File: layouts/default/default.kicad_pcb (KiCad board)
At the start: 2 copper layers, 40.8 x 45.9 mm, 62 parts, among them U10 10µF ±10% 25V X5R, U11 10µF ±10% 25V X5R, U12 10µF ±10% 25V X5R, U13 1MΩ ±1% 62.5mW, U14 100nF ±10% 16V X7R, U16 1µF ±10% 25V X5R, U17 560Ω ±1% 62.5mW, U18 1µF ±10% 25V X5R, U19 4.7kΩ ±1% 62.5mW, U20 10µF ±10% 25V X5R, U21 10µF ±10% 25V X5R, U23 10kΩ ±1% 62.5mW, U25 100nF ±10% 16V X7R, U29 4.7kΩ ±1% 62.5mW, U5 100kΩ ±1% 62.5mW, U6 560kΩ ±1% 62.5mW, U8 1.5µH ±20%, U9 10µF ±10% 25V X5R

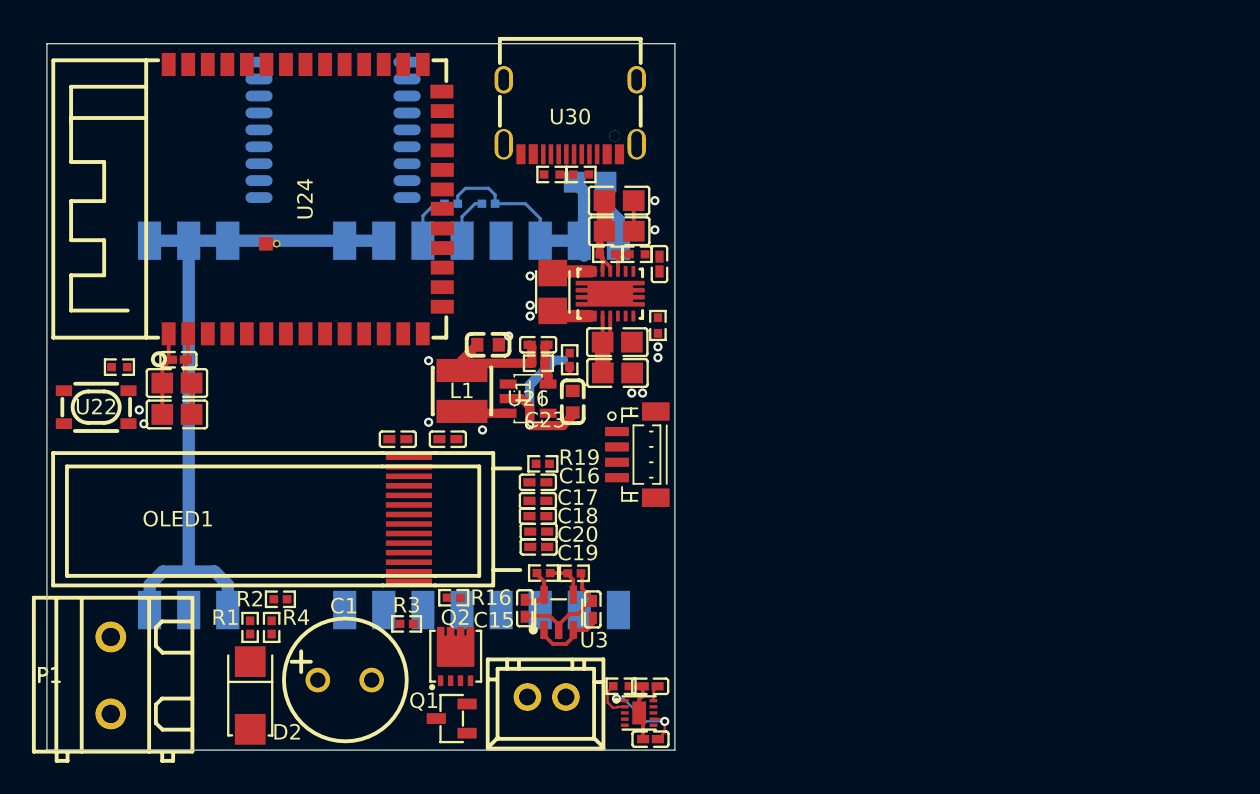
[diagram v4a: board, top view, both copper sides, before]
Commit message: update before removing oled
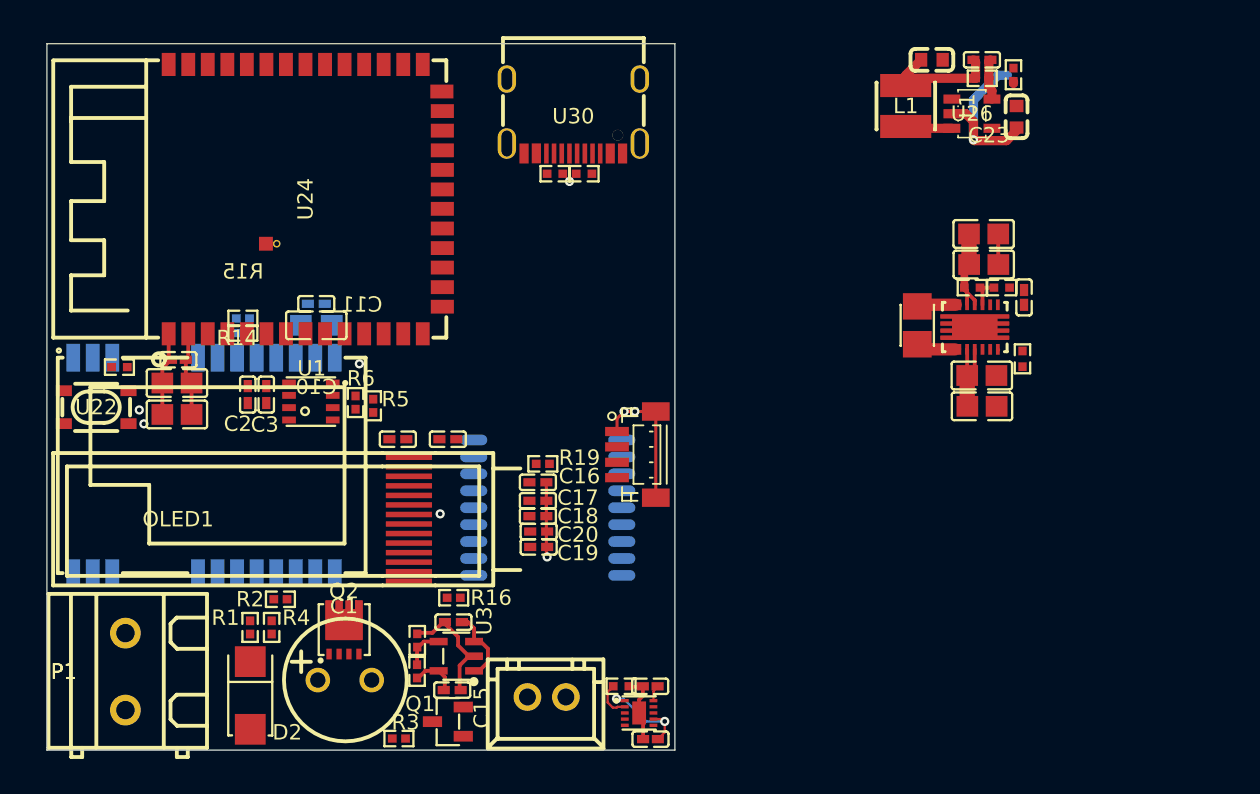
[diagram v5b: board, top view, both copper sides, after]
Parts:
- added C2: 100nF ±10% 16V X7R, atopile:C0402-b3ef17, F.Cu at (46.9, 56.5)
- added C3: 100nF ±10% 16V X7R, atopile:C0402-b3ef17, F.Cu at (48.0, 56.5)
- added R5: 1kΩ ±1% 62.5mW, atopile:R0402-56259e, F.Cu at (55.0, 57.2)
- added R6: 1kΩ ±1% 62.5mW, atopile:R0402-56259e, F.Cu at (53.9, 57.0)
- added U1: , atopile:LGA-8_L3.0-W3.0-P0.80_BME688-7465bb, F.Cu at (51.0, 57.0)
- R1, R14, R15, R2, R3, R4, U5: value 100kΩ ±1% 62.5mW -> 1kΩ ±1% 62.5mW
- R16: value 510kΩ ±1% 62.5mW -> 560kΩ ±1% 62.5mW
- U2: footprint atopile:WIRELM-SMD_E22-900M30S-98c301 -> atopile:WIRELM-SMD_E22-900M22S-72e54e
- U6: value 560kΩ ±1% 62.5mW -> 5.6kΩ ±1% 62.5mW
- moved U26 34.3 mm to (93.9, 38.2)
- moved C22 34.3 mm to (94.5, 34.8)
- moved C23 34.3 mm to (96.8, 38.5)
- moved C24 34.3 mm to (91.3, 34.8)
- moved L1 34.3 mm to (89.6, 37.8)
- moved R20 34.3 mm to (96.6, 35.7)
- moved R21 34.3 mm to (94.6, 36.0)
- moved U27 28.2 mm to (66.3, 63.9)
- moved U10 23.8 mm to (94.6, 57.3)
- moved U11 23.8 mm to (94.7, 48.0)
- moved U13 23.8 mm to (97.2, 54.2)
- moved U14 23.8 mm to (97.3, 50.2)
- moved U5 23.8 mm to (95.8, 49.5)
- moved U9 23.8 mm to (94.5, 55.3)
- moved U12 23.8 mm to (94.7, 46.1)
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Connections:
- C15 pad 1: hv-1 -> hv
- C16 pad 1: hv-3 -> hv-1
- C17 pad 1: hv-3 -> hv-1
- C18 pad 1: hv-3 -> hv-1
- C19 pad 1: hv-3 -> hv-1
- C20 pad 1: hv-3 -> hv-1
- C22 pad 1: hv-3 -> hv-1
- C23 pad 1: hv -> hv-3
- C24 pad 1: hv-3 -> hv-1
- CN1 pad 1: hv -> hv-3
- CN2 pad 2: hv-3 -> hv-1
- L1 pad 2: hv-3 -> hv-1
- OLED1 pad 13: hv-3 -> hv-1
- OLED1 pad 14: hv-3 -> hv-1
- OLED1 pad 5: hv-1 -> hv
- OLED1 pad 8: hv-3 -> hv-1
- R18 pad 1: hv-1 -> hv
- R19 pad 2: hv-3 -> hv-1
- R21 pad 1: hv-3 -> hv-1
- U10 pad 1: hv -> hv-3
- U15 pad 10: hv -> hv-3
- U18 pad 1: hv -> hv-3
- U2 pad 10: hv-2 -> gnd
- U20 pad 1: hv-3 -> hv-1
- U21 pad 1: hv-3 -> hv-1
- U23 pad 1: hv-3 -> hv-1
- U24 pad 2: hv-3 -> hv-1
- U25 pad 1: hv-3 -> hv-1
- U26 pad 4: hv -> hv-3
- U27 pad 14: hv-3 -> hv-1
- U27 pad 8: hv-3 -> hv-1
- U3 pad 5: hv-1 -> hv
- U7 pad 10: hv -> hv-3
- U7 pad 11: hv -> hv-3
- U9 pad 1: hv -> hv-3
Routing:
- net gnd: track 82.0 -> 46.2 mm, vias 16 -> 9
- net hv-2: track 35.5 -> 17.7 mm
- net hv-1: track 3.05 -> 13.5 mm
- net hv-3: track 13.5 -> 6.80 mm
- net RXEN: track 4.05 -> 0.00 mm
- net hv: track 6.80 -> 3.05 mm
- net TXEN: track 3.23 -> 0.00 mm

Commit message: desktop push
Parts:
- removed C12, C13, C14, C15, U16, U18: 1µF ±10% 25V X5R, atopile:C0402-b3ef17
- removed C16, C18, C19, C20, U14: 100nF ±10% 16V X7R, atopile:C0402-b3ef17
- removed C17: 4.7µF ±20% 10V X5R, atopile:C0402-b3ef17
- removed OLED1: , atopile:OLED-SMD_N087-2832TSWYG02-H14_1-7d3a70
- removed R16: 560kΩ ±1% 62.5mW, atopile:R0402-56259e
- removed R17, R19: 10kΩ ±1% 62.5mW, atopile:R0402-56259e
- removed R18: 25.5kΩ ±1% 62.5mW, atopile:R0402-56259e
- removed U1: , atopile:LGA-8_L3.0-W3.0-P0.80_BME688-7465bb
- removed U10, U11, U12, U9: 10µF ±10% 25V X5R, atopile:C0805-3b2e55
- removed U13: 1MΩ ±1% 62.5mW, atopile:R0402-56259e
- removed U15: , lib:WSON-10_L2.0-W2.0-P0.40-BL-EP
- removed U17: 560Ω ±1% 62.5mW, atopile:R0402-56259e
- removed U3: , lib:SOT-23-5_L3.0-W1.7-P0.95-LS2.8-BL
- removed U5: 1kΩ ±1% 62.5mW, atopile:R0402-56259e
- removed U6: 5.6kΩ ±1% 62.5mW, atopile:R0402-56259e
- removed U7: , lib:VSON-14_L4.0-W3.0-P0.50-BL-EP_TI_DSJ
- removed U8: 1.5µH ±20%, lib:IND-SMD_L2.5-W2.0_WPN252012H
- added C4: 100nF ±10% 16V X7R, atopile:C0402-b3ef17, B.Cu at (51.5, 50.5)
- added CN3: , atopile:CONN-SMD_BM04B-SRSS-TB-6963ef, F.Cu at (36.4, 57.1)
- C2: value 100nF ±10% 16V X7R -> 100nF ±10% 50V X7R; footprint atopile:C0402-b3ef17 -> atopile:C0805-3b2e55
- C3: value 100nF ±10% 16V X7R -> 100nF ±10% 50V X7R; footprint atopile:C0402-b3ef17 -> atopile:C0603-bd72f6; moved to B.Cu
- R5: value 1kΩ ±1% 62.5mW -> 10kΩ ±1% 50mW; footprint atopile:R0402-56259e -> atopile:R0201-27027e
- R6: value 1kΩ ±1% 62.5mW -> (none); footprint atopile:R0402-56259e -> atopile:R0201-27027e
- moved C22 50.0 mm to (56.0, 66.7), turned to 90 degrees
- moved C24 49.8 mm to (56.0, 69.9), turned to 90 degrees
- moved R20 49.0 mm to (57.0, 64.6), turned to 180 degrees
- moved R21 48.4 mm to (57.2, 66.6), turned to 90 degrees
- moved L1 45.6 mm to (59.0, 71.6), turned to 0 degrees
- moved C23 45.3 mm to (59.7, 64.4), turned to 0 degrees
- moved U26 45.0 mm to (59.5, 67.3), turned to -90 degrees
- moved CN2 35.9 mm to (36.4, 64.5), turned to 90 degrees
- moved U30 30.6 mm to (66.1, 69.0), turned to 90 degrees
- moved U19 28.3 mm to (62.4, 69.7), turned to 90 degrees
- moved U27 28.1 mm to (44.3, 46.4), turned to 90 degrees
- moved U29 26.0 mm to (62.4, 67.8), turned to -90 degrees
- moved U20 24.7 mm to (62.4, 41.5), turned to 0 degrees
- moved U25 22.9 mm to (62.3, 43.0), turned to 0 degrees
- moved U21 22.8 mm to (58.3, 41.5)
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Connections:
- net B5 renamed CC2
- net CC1 renamed A5
- net DN1 renamed A7
- net DP1 renamed DP2
- net SUB1 renamed A8
- net ldo-FB renamed FB
- C1 pad 2: cutoff-C -> cutoff-C-1
- C10 pad 1: hv-2 -> hv
- C11 pad 1: hv-2 -> hv
- C2 pad 1: hv-1 -> hv-2
- C22 pad 1: hv-1 -> hv
- C23 pad 1: hv-3 -> hv-2
- C24 pad 1: hv-1 -> hv
- C3 pad 1: hv-1 -> hv
- CN1 pad 1: hv-3 -> hv-2
- CN2 pad 2: hv-1 -> hv
- L1 pad 2: hv-1 -> hv
- P1 pad 2: cutoff-C-1 -> cutoff-C
- Q1 pad 3: cutoff-C -> cutoff-C-1
- Q2 pad 5: cutoff-C-1 -> cutoff-C
- R14 pad 1: hv-2 -> hv
- R15 pad 1: hv-2 -> hv
- R21 pad 1: hv-1 -> hv
- R5 pad 1: SCL -> hv
- R5 pad 2: CSB -> TEMP
- R6 pad 1: SDA -> TEMP
- R6 pad 2: CSB -> gnd
- U2 pad 9: hv-2 -> hv
- U20 pad 1: hv-1 -> hv
- U21 pad 1: hv-1 -> hv
- U23 pad 1: hv-1 -> hv
- U24 pad 2: hv-1 -> hv
- U25 pad 1: hv-1 -> hv
- U26 pad 4: hv-3 -> hv-2
- U27 pad 14: hv-1 -> hv
- U27 pad 8: hv-1 -> hv
- U30 pad A4: hv-2 -> hv-1
- U30 pad A9: hv-2 -> hv-1
- U30 pad B4: hv-2 -> hv-1
- U30 pad B9: hv-2 -> hv-1
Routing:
- net gnd: track 46.2 -> 26.7 mm, vias 9 -> 4
- net hv-2: track 17.7 -> 0.00 mm, vias 2 -> 0
- net hv: track 3.05 -> 18.5 mm
- net hv-1: track 13.5 -> 0.00 mm
- net hv-3: track 6.80 -> 0.00 mm
- net ISET: track 2.76 -> 0.00 mm
- net L1: track 2.59 -> 0.00 mm
- net ADJ_NC: track 2.56 -> 0.00 mm
- net L2: track 2.54 -> 0.00 mm
- net boostbuck-FB: track 2.08 -> 0.00 mm
- net (no net): vias 0 -> 4
- added copper zone on In1.Cu, net gnd
- added copper zone on In2.Cu, net gnd
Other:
- board size 40.8 x 45.9 mm -> 37 x 39.2 mm
- copper layers 2 -> 4

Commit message: im cooking
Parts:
- removed P1: , atopile:CONN-TH_2P-P5.00_WJ128V-5.0-2P-75f14f
- added C5: 100nF ±10% 16V X7R, atopile:C0402-b3ef17, F.Cu at (42.6, 65.8)
- added C6: 100nF ±10% 16V X7R, atopile:C0402-b3ef17, F.Cu at (43.6, 65.8)
- added CN4: , atopile:CONN-TH_XH-2A-b4a6f6, F.Cu at (42.8, 75.4)
- added CN5: , atopile:CONN-TH_XH-2A-b4a6f6, F.Cu at (36.5, 75.4)
- added Q3: , atopile:SOT-23-3_L2.9-W1.3-P1.90-LS2.4-BR-688f29, F.Cu at (37.8, 69.8)
- added R7: 10kΩ ±1% 62.5mW, atopile:R0402-56259e, F.Cu at (50.1, 67.3)
- added R8: 10kΩ ±1% 62.5mW, atopile:R0402-56259e, F.Cu at (48.9, 66.5)
- added U1: , atopile:SOP-6_L7.0-W7.0-P2.54-LS10.3-BL-0df1ed, F.Cu at (38.2, 47.0)
- added U3: , atopile:LGA-8_L3.0-W3.0-P0.80_BME688-7465bb, F.Cu at (46.4, 66.6)
- R1, R14, R15, R2, R3, R4: value 1kΩ ±1% 62.5mW -> 10kΩ ±1% 62.5mW
- moved U23 12.5 mm to (41.4, 56.8), turned to 0 degrees
- moved Q2 8.90 mm to (42.9, 69.6), turned to 90 degrees
- moved R3 8.51 mm to (62.2, 72.4), turned to 90 degrees
- moved U22 7.26 mm to (41.3, 60.1), turned to -90 degrees
- moved D2 0.99 mm to (48.0, 76.0)
- moved U30 0.81 mm to (66.4, 68.2)
- moved U19 0.81 mm to (62.7, 69.0)
- moved U29 0.81 mm to (62.7, 67.1)
- moved C1 0.75 mm to (53.8, 75.5)
- moved Q1 0.59 mm to (59.3, 78.0)
- moved CN1 0.56 mm to (66.8, 76.0)
- moved L1 0.32 mm to (59.2, 71.3)
- moved C2 0.25 mm to (60.2, 75.0)
- moved CN2 0.25 mm to (36.4, 64.2)
- moved CN3 0.25 mm to (36.4, 56.9)
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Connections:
- net A8 renamed SUB1
- net SUB2 renamed B8
- net in renamed input
- C1 pad 2: cutoff-C-1 -> cutoff-C
- C10 pad 1: hv -> hv-1
- C11 pad 1: hv -> hv-1
- C2 pad 1: hv-2 -> hv
- C22 pad 1: hv -> hv-1
- C23 pad 1: hv-2 -> hv
- C24 pad 1: hv -> hv-1
- C3 pad 1: hv -> hv-1
- C4 pad 1: hv -> hv-1
- CN1 pad 1: hv-2 -> hv
- CN2 pad 2: hv -> hv-1
- CN3 pad 2: hv -> hv-1
- L1 pad 2: hv -> hv-1
- Q1 pad 3: cutoff-C-1 -> cutoff-C
- Q2 pad 5: cutoff-C -> cutoff-C-2
- R1 pad 1: hv-2 -> hv
- R14 pad 1: hv -> hv-1
- R15 pad 1: hv -> hv-1
- R21 pad 1: hv -> hv-1
- R5 pad 1: hv -> hv-1
- U2 pad 9: hv -> hv-1
- U20 pad 1: hv -> hv-1
- U21 pad 1: hv -> hv-1
- U23 pad 1: hv -> hv-1
- U24 pad 2: hv -> hv-1
- U25 pad 1: hv -> hv-1
- U26 pad 4: hv-2 -> hv
- U27 pad 14: hv -> hv-1
- U27 pad 8: hv -> hv-1
- U30 pad A4: hv-1 -> hv-2
- U30 pad A9: hv-1 -> hv-2
- U30 pad B4: hv-1 -> hv-2
- U30 pad B9: hv-1 -> hv-2
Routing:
- net hv-1: track 0.00 -> 18.5 mm
- net hv: track 18.5 -> 0.00 mm
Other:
- board size 37 x 39.2 mm -> 37 x 39.4 mm

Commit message: im cooking
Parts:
- added GPIO: , atopile:CONN-SMD_7P-P1.00_BM07B-SRSS-TB-201aba, F.Cu at (41.5, 58.0)
- moved R9 7.51 mm to (44.2, 63.8), turned to 180 degrees
- moved RESET 5.92 mm to (41.8, 66.0), turned to 0 degrees
- moved R7 2.85 mm to (53.0, 67.4)
- moved R8 2.85 mm to (51.8, 66.7)
- moved U3 2.85 mm to (49.2, 66.8)
- moved C5 2.85 mm to (45.5, 65.8)
- moved C6 2.85 mm to (46.5, 65.8)
- moved R6 1.07 mm to (54.8, 41.8)
- moved R5 1.07 mm to (53.0, 41.8)
- moved R14 0.71 mm to (46.2, 53.0)
- moved R15 0.70 mm to (47.4, 52.9)
- moved Q3 0.56 mm to (38.0, 69.2)
- moved U1 0.51 mm to (37.8, 46.8)
- moved C2 0.25 mm to (60.2, 74.8)
- moved Q1 0.21 mm to (59.2, 77.8)
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- renumbered CN1 to BATTERY, U21 to C01, U20 to C02, U25 to C03, CN4 to CUTOFF, U24 to ESP32S3, CN5 to HEATER, CN3 to I2C, CN2 to I2C2, U23 to R9, U22 to RESET, U30 to USBC
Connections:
- net A7 renamed DN2
- net CSB renamed VDDIO
- C01 pad 1: hv-1 -> hv-2
- C02 pad 1: hv-1 -> hv-2
- C03 pad 1: hv-1 -> hv-2
- C1 pad 2: cutoff-C -> cutoff-C-1
- C10 pad 1: hv-1 -> hv-2
- C11 pad 1: hv-1 -> hv-2
- C22 pad 1: hv-1 -> hv-2
- C24 pad 1: hv-1 -> hv-2
- C3 pad 1: hv-1 -> hv-2
- C4 pad 1: hv-1 -> hv-2
- C5 pad 1: hv-1 -> hv-2
- C6 pad 1: hv-1 -> hv-2
- CUTOFF pad 2: cutoff-C-2 -> cutoff-C
- ESP32S3 pad 2: hv-1 -> hv-2
- HEATER pad 2: cutoff-C-1 -> cutoff-C-2
- I2C pad 2: hv-1 -> hv-2
- I2C2 pad 2: hv-1 -> hv-2
- L1 pad 2: hv-1 -> hv-2
- Q1 pad 3: cutoff-C -> cutoff-C-1
- Q2 pad 5: cutoff-C-2 -> cutoff-C
- Q3 pad 3: cutoff-C-1 -> cutoff-C-2
- R14 pad 1: hv-1 -> hv-2
- R15 pad 1: hv-1 -> hv-2
- R21 pad 1: hv-1 -> hv-2
- R5 pad 1: hv-1 -> hv-2
- R9 pad 1: hv-1 -> hv-2
- U1 pad 2: hv-1 -> hv-2
- U2 pad 9: hv-1 -> hv-2
- U27 pad 14: hv-1 -> hv-2
- U27 pad 8: hv-1 -> hv-2
- U3 pad 8: hv-1 -> hv-2
- USBC pad A4: hv-2 -> hv-1
- USBC pad A9: hv-2 -> hv-1
- USBC pad B4: hv-2 -> hv-1
- USBC pad B9: hv-2 -> hv-1
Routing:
- net hv-2: track 0.00 -> 18.5 mm
- net hv-1: track 18.5 -> 0.00 mm
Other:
- board size 37 x 39.4 mm -> 37.6 x 39.4 mm
